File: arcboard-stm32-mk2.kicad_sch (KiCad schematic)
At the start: 75 parts, among them J1 Conn_01x04_Socket, J17 Conn_01x04_Socket, J2 Conn_01x04_Socket, J3 Conn_01x04_Socket, J4 Conn_01x04_Socket, J5 Conn_01x02_Socket, U1 XC6210B332MR-G, U13 2N7002, U14 W25Q128JVSIQTR, U15 TS-1187A-B-A-B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

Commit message: starting readme, added haptic
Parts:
- removed J4: Conn_01x04_Socket, Connector_PinSocket_1.00mm:PinSocket_1x04_P1.00mm_Vertical, symbol Connector:Conn_01x04_Socket
- removed LOGO6: **REF, kicad-libraries:cyboard-logo-5mm, symbol kicad-libraries:qmk-lite-logo
- added C2, C4: 1uF, Capacitor_SMD:C_0402_1005Metric, symbol Device:C
- added J6: Conn_01x02_Socket, Connector_PinHeader_1.00mm:PinHeader_1x02_P1.00mm_Vertical, symbol Connector:Conn_01x02_Socket
- added J7: Conn_01x02_Socket, Connector_JST:JST_PH_S2B-PH-K_1x02_P2.00mm_Horizontal, symbol Connector:Conn_01x02_Socket
- added R13, R4: 0402WGF2201TCE, kicad-libraries:R0402, symbol kicad-libraries:0402WGF2201TCE
- added U5: DRV2605LDGSR, kicad-libraries:VSSOP-10_L3.0-W3.0-P0.50-LS4.9-BL, symbol kicad-libraries:DRV2605LDGSR
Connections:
- net SPARE4 is gone; now on net LED_SIG_OUTPUT: U2.66 (PC9)
- net +3V3: now also C4.1, R13.2, R4.2, U5.10 (VDD), U5.5 (EN)
- net GND: now also C2.1, C4.2, U5.8 (GND)
- net LCD_BL: now also U2.36 (PB1); no longer U2.34 (PC5)
- net LED_SIG_OUTPUT: no longer U2.79 (PC11)
- net HAPTIC_PWM: now reaches U2.38 (PE7)
- net HAPTIC_PWM: now also U5.4 (IN/TRIG)
- net I2C_SCL: now reaches U2.47 (PB10)
- net I2C_SCL: now also J6.1 (Pin_1), R13.1, U5.2 (SCL)
- net I2C_SDA: now reaches U2.48 (PB11)
- net I2C_SDA: now also J6.2 (Pin_2), R4.1, U5.3 (SDA)
- net SPARE1: no longer names the net of U2.63 (PC6)
- net SPARE2: no longer names the net of U2.64 (PC7)
- net SPARE3: no longer names the net of U2.65 (PC8)
- new net: C2.2, U5.1 (REG)
- new net HAPTIC_neg: J7.1 (Pin_1), U5.9 (OUT-)
- new net HAPTIC_pos: J7.2 (Pin_2), U5.7 (OUT+)
- no-connect marks 36 -> 34
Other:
- note added: "60-pin connector"
- note added: "DFU, RESET, BOOT"
- note added: "I2C for haptic"
- note added: "TIM1"
- note added: "TIM3"
- note removed: "DFU, RESET, BOOT Buttons"
- note removed: "RGB LEDs"
- note removed: "Spare pins"
- moved on the sheet: C1, C10, C11, C12, C13, C14, C15, C16, C17, C18, C19, C20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

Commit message: finishing haptic bits
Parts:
- added U6: PAM8302AASCR, kicad-libraries:MSOP-8_L3.0-W3.0-P0.65-LS5.0-BL, symbol kicad-libraries:PAM8302AASCR
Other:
- note added: "re-route motion to a pad & spare pin"
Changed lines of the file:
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@@
 		)
 	)
+	(text "re-route motion to a pad & spare pin"
+		(exclude_from_sim no)
+		(at 428.498 168.148 0)
+		(effects
+			(font
+				(size 1.27 1.27)
+			)
+		)
+	)
 	(text "60-pin connector"
 		(exclude_from_sim no)
@@
 					(unit 1)
 				)
+			)
+		)
+	)
+	(symbol
+		(lib_id "kicad-libraries:PAM8302AASCR")
+		(at 308.61 356.87 0)
+		(unit 1)
+		(exclude_from_sim yes)
+		(in_bom no)
+		(on_board no)
+		(dnp yes)
+		(fields_autoplaced yes)
+		(property "Reference" "U6"
+			(at 310.2611 345.44 0)
+			(effects
+				(font
+					(size 1.27 1.27)
+				)
+				(justify left)
+			)
+		)
+		(property "Value" "PAM8302AASCR"
+			(at 310.2611 347.98 0)
+			(effects
+				(font
+					(size 1.27 1.27)
+				)
+				(justify left)
+			)
+		)
+		(property "Footprint" "kicad-libraries:MSOP-8_L3.0-W3.0-P0.65-LS5.0-BL"
+			(at 308.61 367.03 0)
+			(effects
+				(font
+					(size 1.27 1.27)
+					(italic yes)
+				)
+				(hide yes)
+			)
+		)
+		(property "Datasheet" "https://item.szlcsc.com/118796.html"
+			(at 306.324 356.743 0)
+			(effects
+				(font
+					(size 1.27 1.27)
+				)
+				(justify left)
+				(hide yes)
+			)
+		)
+		(property "Description" ""
+			(at 308.61 356.87 0)
+			(effects
+				(font
+					(size 1.27 1.27)
+				)
+				(hide yes)
+			)
+		)
+		(property "LCSC" "C113367"
+			(at 308.61 356.87 0)
+			(effects
+				(font
+					(size 1.27 1.27)
+				)
+				(hide yes)
+			)
+		)
+		(pin "2"
+		)
+		(pin "1"
+		)
+		(pin "3"
+		)
+		(pin "8"
+		)
+		(pin "6"
+		)
+		(pin "7"
+		)
+		(pin "5"
+		)
+		(pin "8"
+		)
+		(instances
+			(project ""
+				(path "/e3b5a64c-dc86-4c04-b1b0-762b30a6a8fe"
+					(reference "U6")
+					(unit 1)
+				)

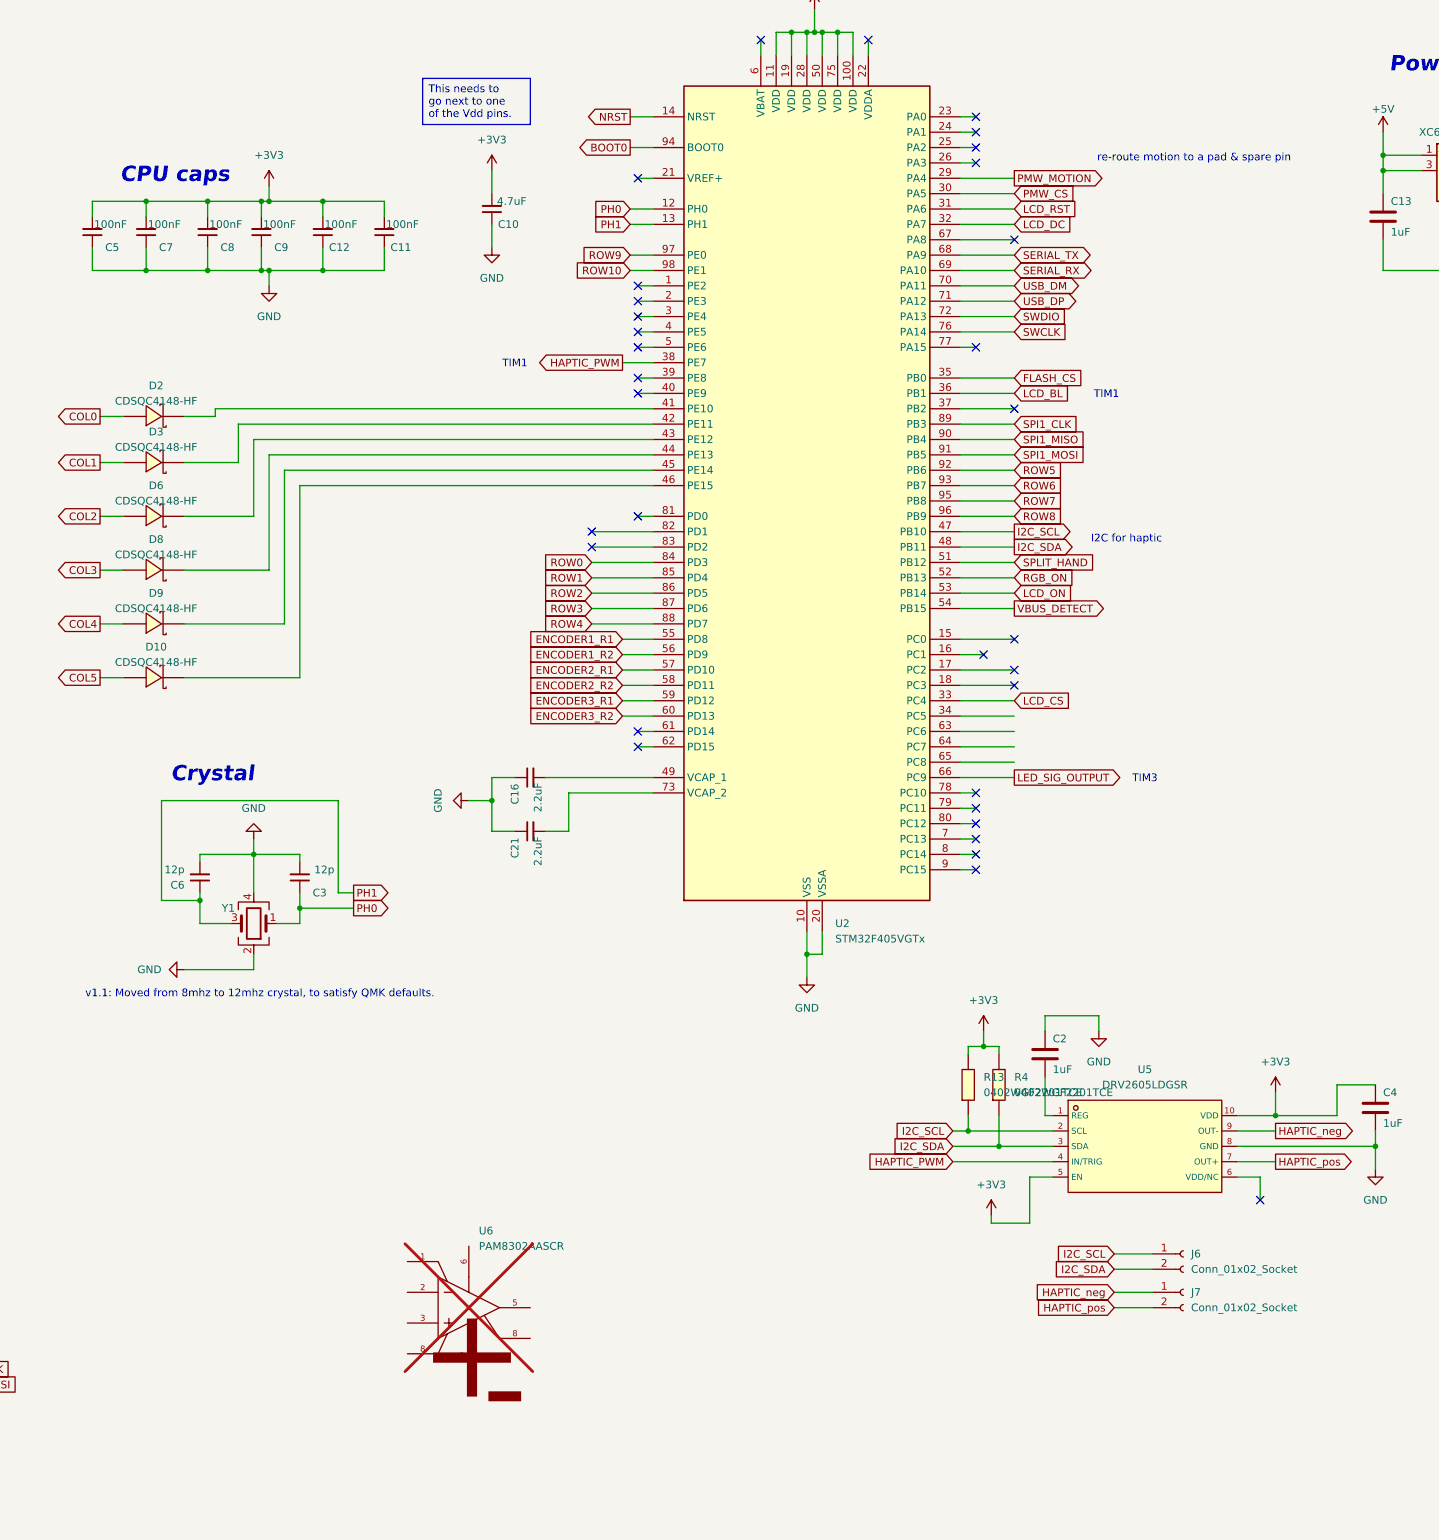
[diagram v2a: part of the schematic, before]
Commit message: adding dac amp
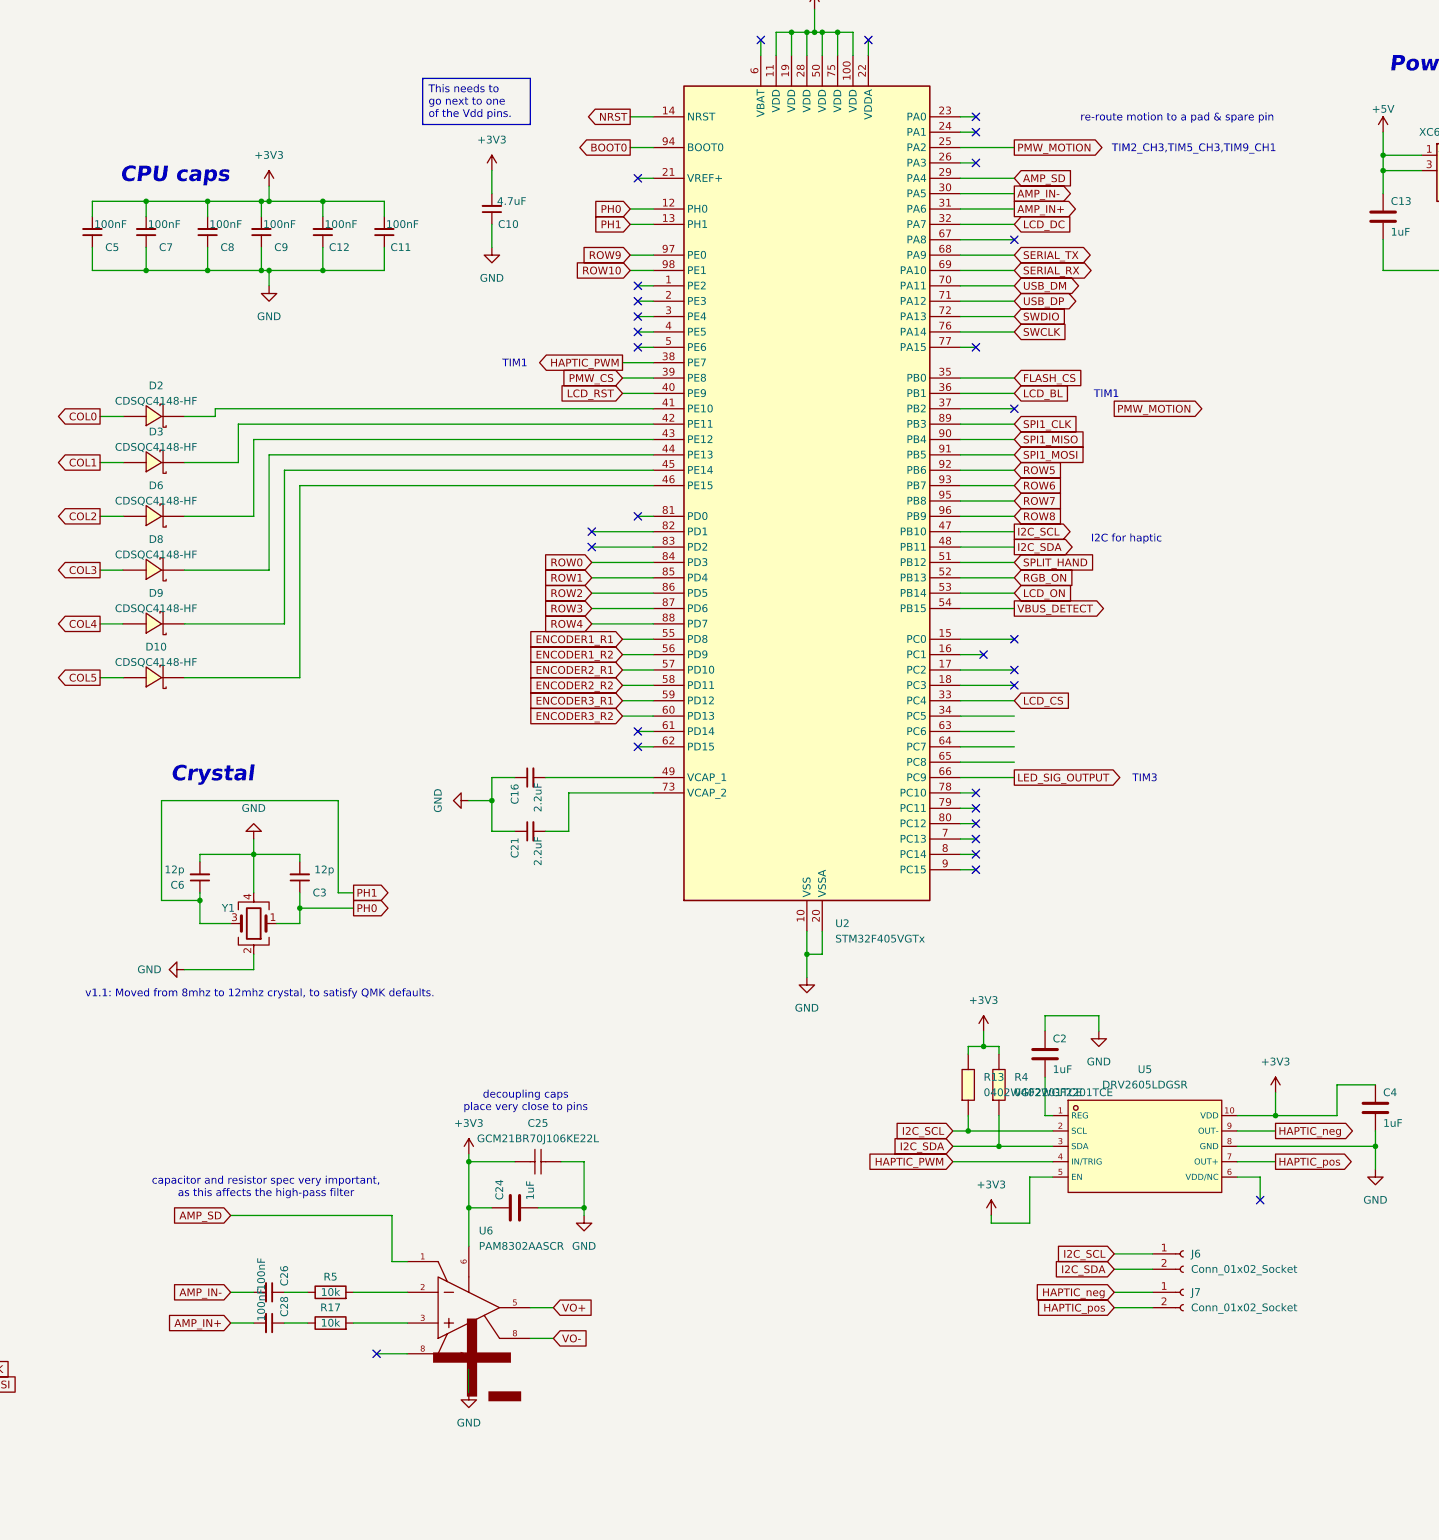
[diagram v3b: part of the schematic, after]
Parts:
- added C24: 1uF, Capacitor_SMD:C_0402_1005Metric, symbol Device:C
- added C25: GCM21BR70J106KE22L, kicad-libraries:C0805, symbol kicad-libraries:GCM21BR70J106KE22L
- added C26, C28: 100nF, Capacitor_SMD:C_0402_1005Metric, symbol Device:C_Small
- added R17, R5: 10k, Resistor_SMD:R_0402_1005Metric, symbol Device:R
- U6: now fitted; now in the parts list
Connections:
- net +3V3: now also U6.6 (VDD), C24.1, C25.1
- net GND: now also U6.7 (GND), C24.2, C25.2
- net LCD_RST: now also U2.40 (PE9); no longer U2.31 (PA6)
- net PMW_CS: now also U2.39 (PE8); no longer U2.30 (PA5)
- net PMW_MOTION: now also U2.25 (PA2); no longer U2.29 (PA4)
- net AMP_SD: now reaches U6.1 (SD#)
- net AMP_SD: now also U2.29 (PA4)
- net at U6.2 (IN-): now also R5.2
- net at U6.3 (IN+): now also R17.2
- net VO+: now reaches U6.5 (VO+)
- net VO-: now reaches U6.8 (VO-)
- new net: C26.1, R5.1
- new net: C28.1, R17.1
- new net AMP_IN+: C28.2, U2.31 (PA6)
- new net AMP_IN-: C26.2, U2.30 (PA5)
- no-connect marks 34 -> 32
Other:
- note added: "TIM2_CH3,TIM5_CH3,TIM9_CH1"
- note added: "capacitor and resistor spec very important, as this affects the high-pass filter"
- note added: "decoupling caps place very close to pins"

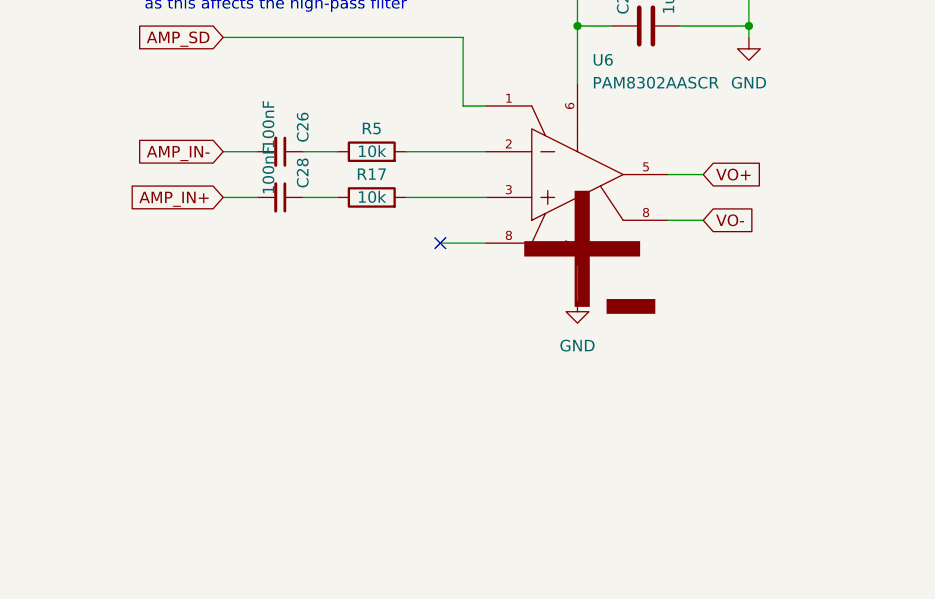
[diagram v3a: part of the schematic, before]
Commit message: adding piezo that does not fit
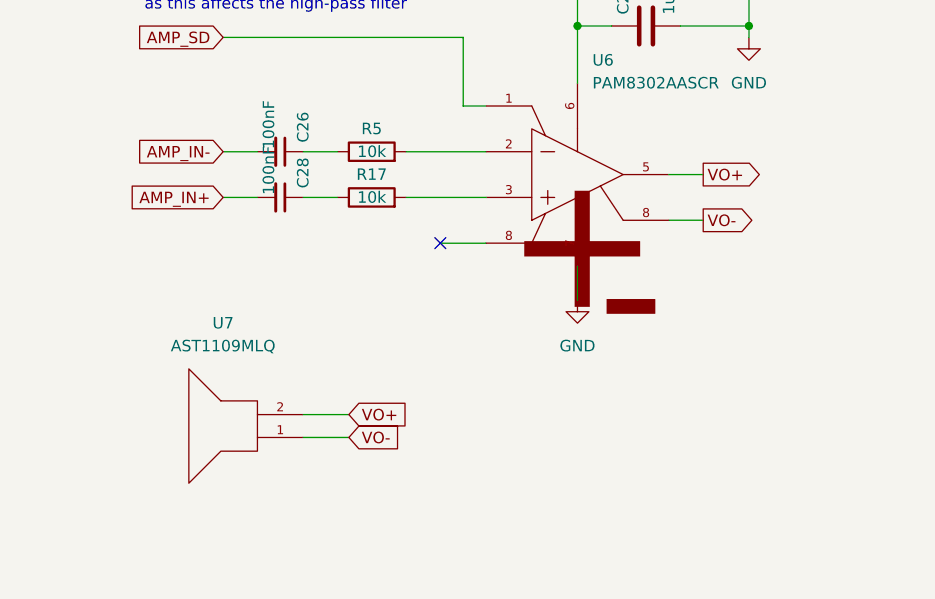
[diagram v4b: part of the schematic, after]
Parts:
- added U7: AST1109MLQ, kicad-libraries:BUZ-SMD_L11.0-W9.0, symbol kicad-libraries:AST1109MLQ
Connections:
- net VO+: now also U7.2
- net VO-: now also U7.1
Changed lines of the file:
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@@
 	(wire
 		(pts
+			(xy 278.13 387.35) (xy 283.21 387.35)
+		)
+		(stroke
+			(width 0)
+			(type default)
+		)
+	)
+	(wire
+		(pts
 			(xy 45.72 331.47) (xy 55.88 331.47)
 		)
@@
 	(wire
 		(pts
+			(xy 278.13 384.81) (xy 283.21 384.81)
+		)
+		(stroke
+			(width 0)
+			(type default)
+		)
+	)
+	(wire
+		(pts
 			(xy 270.51 212.09) (xy 339.09 212.09)
 		)
@@
 	)
 	(global_label "VO-"
-		(shape input)
+		(shape output)
 		(at 322.58 363.22 0)
 		(fields_autoplaced yes)
@@
 	)
 	(global_label "VO+"
-		(shape input)
+		(shape output)
 		(at 322.58 358.14 0)
 		(fields_autoplaced yes)
@@
 		)
 	)
+	(global_label "VO+"
+		(shape input)
+		(at 283.21 384.81 0)
+		(fields_autoplaced yes)
+		(effects
+			(font
+				(size 1.27 1.27)
+			)
+			(justify left)
+		)
+		(property "Intersheetrefs" "${INTERSHEET_REFS}"
+			(at 290.1867 384.81 0)
+			(effects
+				(font
+					(size 1.27 1.27)
+				)
+				(justify left)
+				(hide yes)
+			)
+		)
+	)
 	(global_label "ROW0"
 		(shape input)
@@
 		)
 	)
+	(global_label "VO-"
+		(shape input)
+		(at 283.21 387.35 0)
+		(fields_autoplaced yes)
+		(effects
+			(font
+				(size 1.27 1.27)
+			)
+			(justify left)
+		)
+		(property "Intersheetrefs" "${INTERSHEET_REFS}"
+			(at 290.1867 387.35 0)
+			(effects
+				(font
+					(size 1.27 1.27)
+				)
+				(justify left)
+				(hide yes)
+			)
+		)
+	)
 	(global_label "AMP_IN+"
 		(shape input)
@@
 					(unit 1)
 				)
+			)
+		)
+	)
+	(symbol
+		(lib_id "kicad-libraries:AST1109MLQ")
+		(at 273.05 387.35 0)
+		(unit 1)
+		(exclude_from_sim no)
+		(in_bom yes)
+		(on_board yes)
+		(dnp no)
+		(fields_autoplaced yes)
+		(property "Reference" "U7"
+			(at 269.24 374.65 0)
+			(effects
+				(font
+					(size 1.27 1.27)
+				)
+			)
+		)
+		(property "Value" "AST1109MLQ"
+			(at 269.24 377.19 0)
+			(effects
+				(font
+					(size 1.27 1.27)
+				)
+			)
+		)
+		(property "Footprint" "kicad-libraries:BUZ-SMD_L11.0-W9.0"
+			(at 273.05 397.51 0)
+			(effects
+				(font
+					(size 1.27 1.27)
+					(italic yes)
+				)
+				(hide yes)
+			)
+		)
+		(property "Datasheet" "https://item.szlcsc.com/1056289.html"
+			(at 270.764 387.223 0)
+			(effects
+				(font
+					(size 1.27 1.27)
+				)
+				(justify left)
+				(hide yes)
+			)
+		)
+		(property "Description" ""
+			(at 273.05 387.35 0)
+			(effects
+				(font
+					(size 1.27 1.27)
+				)
+				(hide yes)
+			)
+		)
+		(property "LCSC" "C9900020429"
+			(at 273.05 387.35 0)
+			(effects
+				(font
+					(size 1.27 1.27)
+				)
+				(hide yes)
+			)
+		)
+		(pin "2"
+		)
+		(pin "1"
+		)
+		(instances
+			(project ""
+				(path "/e3b5a64c-dc86-4c04-b1b0-762b30a6a8fe"
+					(reference "U7")
+					(unit 1)
+				)
